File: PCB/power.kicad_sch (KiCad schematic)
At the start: 0 parts

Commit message: Add power supplies
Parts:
- added C27, C30, C33: 10µF, Capacitor_SMD:C_0805_2012Metric, symbol Device:C
- added C28, C29, C31, C32, C34, C35: 22µF, Capacitor_SMD:C_0805_2012Metric, symbol Device:C
- added L1, L2, L3: 2.2µH, Inductor_SMD:L_1210_3225Metric, symbol Device:L
- added R10: 4.75kΩ, Resistor_SMD:R_0402_1005Metric_Pad0.72x0.64mm_HandSolder, symbol Device:R
- added R11: 1.5kΩ, Resistor_SMD:R_0402_1005Metric_Pad0.72x0.64mm_HandSolder, symbol Device:R
- added R12: 1.37kΩ, Resistor_SMD:R_0402_1005Metric_Pad0.72x0.64mm_HandSolder, symbol Device:R
- added R13: 1.65kΩ, Resistor_SMD:R_0402_1005Metric_Pad0.72x0.64mm_HandSolder, symbol Device:R
- added R8: 11.5kΩ, Resistor_SMD:R_0402_1005Metric_Pad0.72x0.64mm_HandSolder, symbol Device:R
- added R9: 2.55kΩ, Resistor_SMD:R_0402_1005Metric_Pad0.72x0.64mm_HandSolder, symbol Device:R
- added U3, U4, U5: TLV62569DBVR, Package_TO_SOT_SMD:SOT-23-5, symbol Regulator_Switching:TLV62569DBV
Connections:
- new net: L3.1, U5.3 (SW)
- new net: L1.1, U3.3 (SW)
- new net: R8.2, R9.1, U3.5 (FB)
- new net: L2.1, U4.3 (SW)
- new net: R10.2, R11.1, U4.5 (FB)
- new net: R12.2, R13.1, U5.5 (FB)
- new net +1V1: C34.1, C35.1, L3.2, R12.1
- new net +2V5: C31.1, C32.1, L2.2, R10.1
- new net +3V3: C28.1, C29.1, L1.2, R8.1
- new net GND: C27.2, C28.2, C29.2, C30.2, C31.2, C32.2, C33.2, C34.2, C35.2, R11.2, R13.2, R9.2, U3.2 (GND), U4.2 (GND), U5.2 (GND)
- new net VBUS: C27.1, C30.1, C33.1, U3.1 (EN), U3.4 (VIN), U4.1 (EN), U4.4 (VIN), U5.1 (EN), U5.4 (VIN)

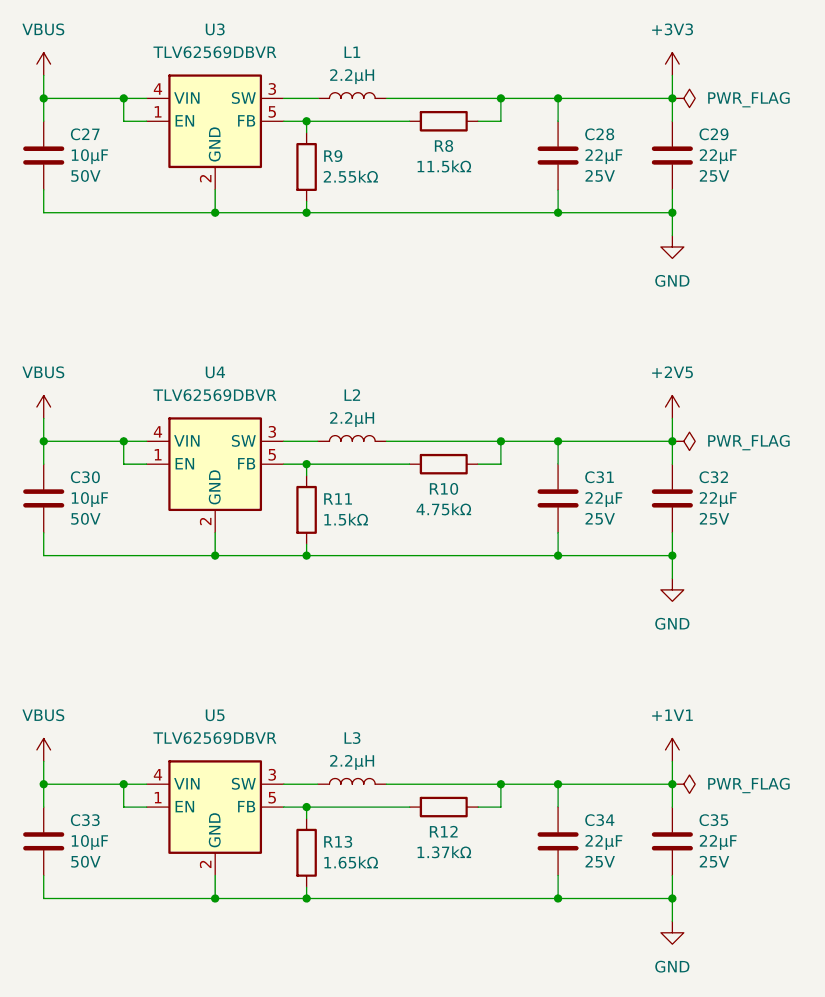
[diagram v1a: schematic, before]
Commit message: Add a USB hub
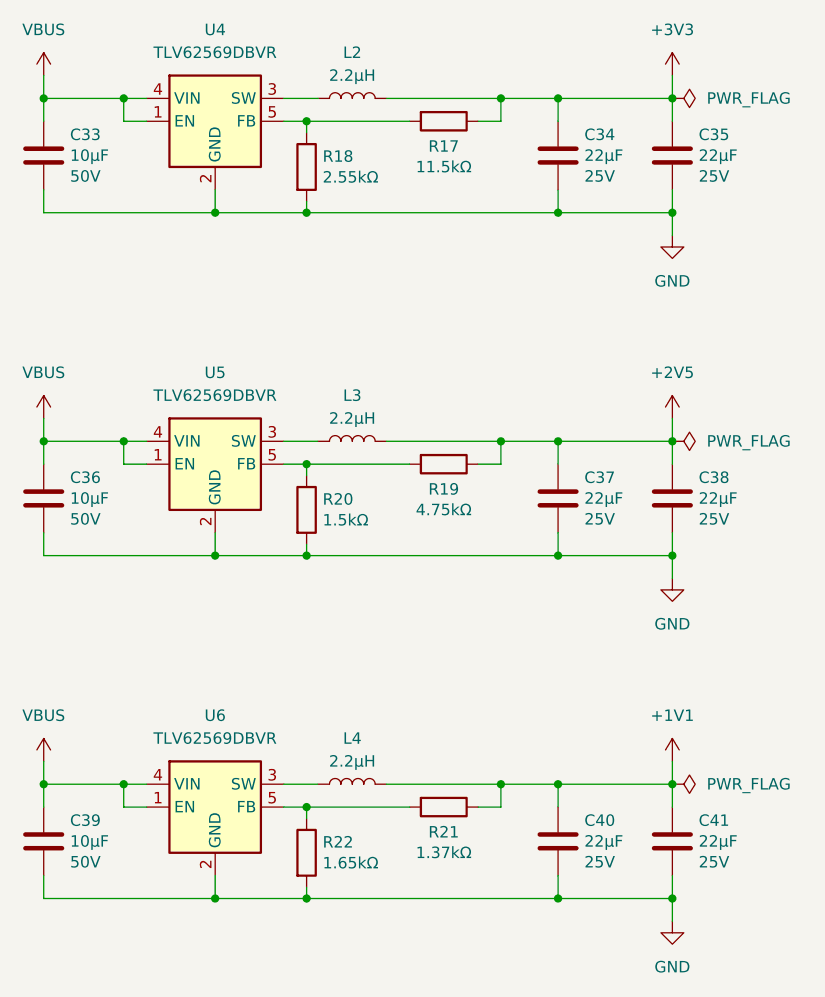
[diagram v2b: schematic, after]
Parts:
- renumbered C27 to C33, C28 to C34, C29 to C35, C30 to C36, C31 to C37, C32 to C38, C33 to C39, C34 to C40, C35 to C41, L1 to L2, L2 to L3, L3 to L4, R8 to R17, R9 to R18, R10 to R19, R11 to R20, R12 to R21, R13 to R22, U3 to U4, U4 to U5, U5 to U6

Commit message: Add the USB to JTAG bridge
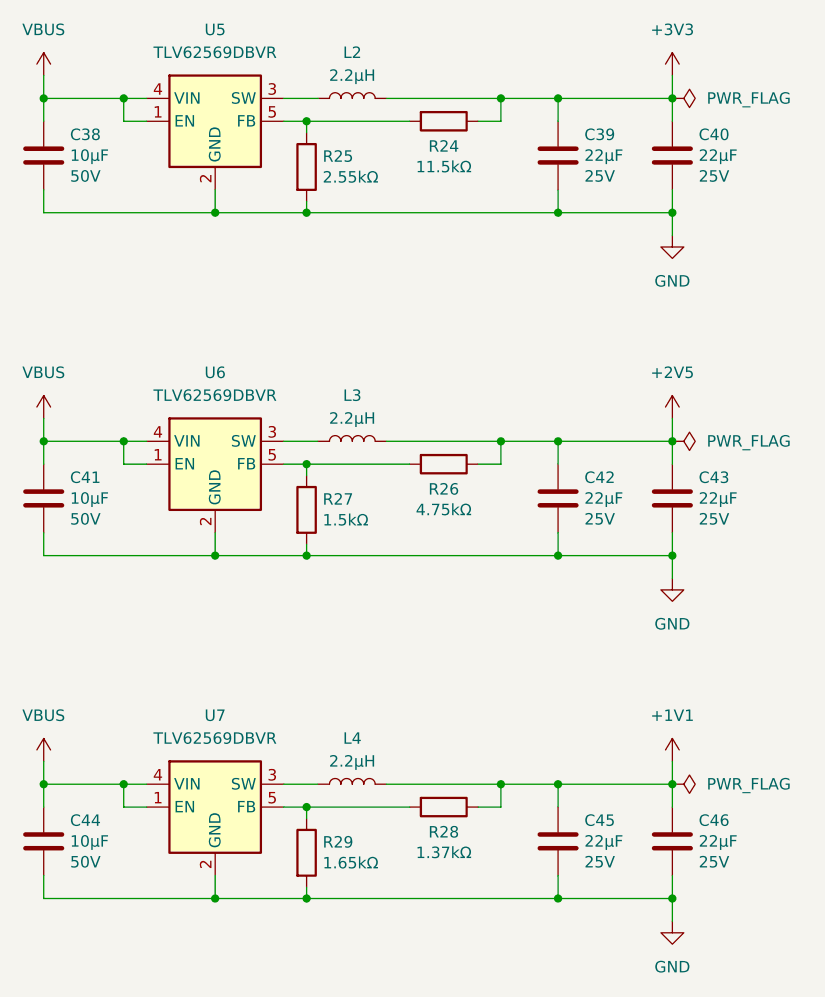
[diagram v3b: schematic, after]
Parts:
- renumbered C33 to C38, C34 to C39, C35 to C40, C36 to C41, C37 to C42, C38 to C43, C39 to C44, C40 to C45, C41 to C46, R17 to R24, R18 to R25, R19 to R26, R20 to R27, R21 to R28, R22 to R29, U4 to U5, U5 to U6, U6 to U7
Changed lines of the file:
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@@
 		(dnp no)
 		(fields_autoplaced yes)
-		(property "Reference" "#PWR060"
+		(property "Reference" "#PWR071"
 			(at 171.45 110.49 0)
 			(effects
@@
 			(project "clavier"
 				(path "/6362c6e0-59ef-40d3-b6e0-7e9dfe7b9b20/0c8a9398-ddd2-4230-9850-fe0f46e922ad"
-					(reference "#PWR060")
+					(reference "#PWR071")
 					(unit 1)
 				)
@@
 		(dnp no)
 		(fields_autoplaced yes)
-		(property "Reference" "U4"
+		(property "Reference" "U5"
 			(at 120.65 43.18 0)
 			(effects
@@
 			(project ""
 				(path "/6362c6e0-59ef-40d3-b6e0-7e9dfe7b9b20/0c8a9398-ddd2-4230-9850-fe0f46e922ad"
-					(reference "U4")
+					(reference "U5")
 					(unit 1)
 				)
@@
 		(dnp no)
 		(fields_autoplaced yes)
-		(property "Reference" "#PWR057"
+		(property "Reference" "#PWR068"
 			(at 171.45 72.39 0)
 			(effects
@@
 			(project "clavier"
 				(path "/6362c6e0-59ef-40d3-b6e0-7e9dfe7b9b20/0c8a9398-ddd2-4230-9850-fe0f46e922ad"
-					(reference "#PWR057")
+					(reference "#PWR068")
 					(unit 1)
 				)
@@
 		(on_board yes)
 		(dnp no)
-		(property "Reference" "R17"
+		(property "Reference" "R24"
 			(at 146.05 56.134 90)
 			(effects
@@
 			(project "clavier"
 				(path "/6362c6e0-59ef-40d3-b6e0-7e9dfe7b9b20/0c8a9398-ddd2-4230-9850-fe0f46e922ad"
-					(reference "R17")
+					(reference "R24")
 					(unit 1)
 				)
@@
 		(dnp no)
 		(fields_autoplaced yes)
-		(property "Reference" "U5"
+		(property "Reference" "U6"
 			(at 120.65 81.28 0)
 			(effects
@@
 			(project "clavier"
 				(path "/6362c6e0-59ef-40d3-b6e0-7e9dfe7b9b20/0c8a9398-ddd2-4230-9850-fe0f46e922ad"
-					(reference "U5")
+					(reference "U6")
 					(unit 1)
 				)
@@
 		(on_board yes)
 		(dnp no)
-		(property "Reference" "C35"
+		(property "Reference" "C40"
 			(at 174.371 54.8386 0)
 			(effects
@@
 			(project "clavier"
 				(path "/6362c6e0-59ef-40d3-b6e0-7e9dfe7b9b20/0c8a9398-ddd2-4230-9850-fe0f46e922ad"
-					(reference "C35")
+					(reference "C40")
 					(unit 1)
 				)
@@
 		(dnp no)
 		(fields_autoplaced yes)
-		(property "Reference" "U6"
+		(property "Reference" "U7"
 			(at 120.65 119.38 0)
 			(effects
@@
 			(project "clavier"
 				(path "/6362c6e0-59ef-40d3-b6e0-7e9dfe7b9b20/0c8a9398-ddd2-4230-9850-fe0f46e922ad"
-					(reference "U6")
+					(reference "U7")
 					(unit 1)
 				)
@@
 		(on_board yes)
 		(dnp no)
-		(property "Reference" "C37"
+		(property "Reference" "C42"
 			(at 161.671 92.9386 0)
 			(effects
@@
 			(project "clavier"
 				(path "/6362c6e0-59ef-40d3-b6e0-7e9dfe7b9b20/0c8a9398-ddd2-4230-9850-fe0f46e922ad"
-					(reference "C37")
+					(reference "C42")
 					(unit 1)
 				)
@@
 		(dnp no)
 		(fields_autoplaced yes)
-		(property "Reference" "#PWR061"
+		(property "Reference" "#PWR072"
 			(at 101.6 128.27 0)
 			(effects
@@
 			(project "clavier"
 				(path "/6362c6e0-59ef-40d3-b6e0-7e9dfe7b9b20/0c8a9398-ddd2-4230-9850-fe0f46e922ad"
-					(reference "#PWR061")
+					(reference "#PWR072")
 					(unit 1)
 				)
@@
 		(on_board yes)
 		(dnp no)
-		(property "Reference" "C33"
+		(property "Reference" "C38"
 			(at 104.521 54.8386 0)
 			(effects
@@
 			(project "clavier"
 				(path "/6362c6e0-59ef-40d3-b6e0-7e9dfe7b9b20/0c8a9398-ddd2-4230-9850-fe0f46e922ad"
-					(reference "C33")
+					(reference "C38")
 					(unit 1)
 				)
@@
 		(dnp no)
 		(fields_autoplaced yes)
-		(property "Reference" "#PWR063"
+		(property "Reference" "#PWR074"
 			(at 171.45 148.59 0)
 			(effects
@@
 			(project "clavier"
 				(path "/6362c6e0-59ef-40d3-b6e0-7e9dfe7b9b20/0c8a9398-ddd2-4230-9850-fe0f46e922ad"
-					(reference "#PWR063")
+					(reference "#PWR074")
 					(unit 1)
 				)
@@
 		(dnp no)
 		(fields_autoplaced yes)
-		(property "Reference" "#PWR055"
+		(property "Reference" "#PWR066"
 			(at 101.6 52.07 0)
 			(effects
@@
 			(project ""
 				(path "/6362c6e0-59ef-40d3-b6e0-7e9dfe7b9b20/0c8a9398-ddd2-4230-9850-fe0f46e922ad"
-					(reference "#PWR055")
+					(reference "#PWR066")
 					(unit 1)
 				)
@@
 		(on_board yes)
 		(dnp no)
-		(property "Reference" "R19"
+		(property "Reference" "R26"
 			(at 146.05 94.234 90)
 			(effects
@@
 			(project "clavier"
 				(path "/6362c6e0-59ef-40d3-b6e0-7e9dfe7b9b20/0c8a9398-ddd2-4230-9850-fe0f46e922ad"
-					(reference "R19")
+					(reference "R26")
 					(unit 1)
 				)
@@
 		(on_board yes)
 		(dnp no)
-		(property "Reference" "R21"
+		(property "Reference" "R28"
 			(at 146.05 132.334 90)
 			(effects
@@
 			(project "clavier"
 				(path "/6362c6e0-59ef-40d3-b6e0-7e9dfe7b9b20/0c8a9398-ddd2-4230-9850-fe0f46e922ad"
-					(reference "R21")
+					(reference "R28")
 					(unit 1)
 				)
@@
 		(dnp no)
 		(fields_autoplaced yes)
-		(property "Reference" "#PWR058"
+		(property "Reference" "#PWR069"
 			(at 101.6 90.17 0)
 			(effects
@@
 			(project "clavier"
 				(path "/6362c6e0-59ef-40d3-b6e0-7e9dfe7b9b20/0c8a9398-ddd2-4230-9850-fe0f46e922ad"
-					(reference "#PWR058")
+					(reference "#PWR069")
 					(unit 1)
 				)
@@
 		(on_board yes)
 		(dnp no)
-		(property "Reference" "R20"
+		(property "Reference" "R27"
 			(at 132.588 95.3516 0)
 			(effects
@@
 			(project "clavier"
 				(path "/6362c6e0-59ef-40d3-b6e0-7e9dfe7b9b20/0c8a9398-ddd2-4230-9850-fe0f46e922ad"
-					(reference "R20")
+					(reference "R27")
 					(unit 1)
 				)
@@
 		(on_board yes)
 		(dnp no)
-		(property "Reference" "C41"
+		(property "Reference" "C46"
 			(at 174.371 131.0386 0)
 			(effects
@@
 			(project "clavier"
 				(path "/6362c6e0-59ef-40d3-b6e0-7e9dfe7b9b20/0c8a9398-ddd2-4230-9850-fe0f46e922ad"
-					(reference "C41")
+					(reference "C46")
 					(unit 1)
 				)
@@
 		(dnp no)
 		(fields_autoplaced yes)
-		(property "Reference" "#PWR056"
+		(property "Reference" "#PWR067"
 			(at 171.45 52.07 0)
 			(effects
@@
 			(project "clavier"
 				(path "/6362c6e0-59ef-40d3-b6e0-7e9dfe7b9b20/0c8a9398-ddd2-4230-9850-fe0f46e922ad"
-					(reference "#PWR056")
+					(reference "#PWR067")
 					(unit 1)
 				)
@@
 		(on_board yes)
 		(dnp no)
-		(property "Reference" "C40"
+		(property "Reference" "C45"
 			(at 161.671 131.0386 0)
 			(effects
@@
 			(project "clavier"
 				(path "/6362c6e0-59ef-40d3-b6e0-7e9dfe7b9b20/0c8a9398-ddd2-4230-9850-fe0f46e922ad"
-					(reference "C40")
+					(reference "C45")
 					(unit 1)
 				)
@@
 		(dnp no)
 		(fields_autoplaced yes)
-		(property "Reference" "#PWR062"
+		(property "Reference" "#PWR073"
 			(at 171.45 128.27 0)
 			(effects
@@
 			(project "clavier"
 				(path "/6362c6e0-59ef-40d3-b6e0-7e9dfe7b9b20/0c8a9398-ddd2-4230-9850-fe0f46e922ad"
-					(reference "#PWR062")
+					(reference "#PWR073")
 					(unit 1)
 				)
@@
 		(on_board yes)
 		(dnp no)
-		(property "Reference" "C34"
+		(property "Reference" "C39"
 			(at 161.671 54.8386 0)
 			(effects
@@
 			(project "clavier"
 				(path "/6362c6e0-59ef-40d3-b6e0-7e9dfe7b9b20/0c8a9398-ddd2-4230-9850-fe0f46e922ad"
-					(reference "C34")
+					(reference "C39")
 					(unit 1)
 				)
@@
 		(on_board yes)
 		(dnp no)
-		(property "Reference" "R22"
+		(property "Reference" "R29"
 			(at 132.588 133.4516 0)
 			(effects
@@
 			(project "clavier"
 				(path "/6362c6e0-59ef-40d3-b6e0-7e9dfe7b9b20/0c8a9398-ddd2-4230-9850-fe0f46e922ad"
-					(reference "R22")
+					(reference "R29")
 					(unit 1)
 				)
@@
 		(on_board yes)
 		(dnp no)
-		(property "Reference" "R18"
+		(property "Reference" "R25"
 			(at 132.588 57.2516 0)
 			(effects
@@
 			(project "clavier"
 				(path "/6362c6e0-59ef-40d3-b6e0-7e9dfe7b9b20/0c8a9398-ddd2-4230-9850-fe0f46e922ad"
-					(reference "R18")
+					(reference "R25")
 					(unit 1)
 				)
@@
 		(on_board yes)
 		(dnp no)
-		(property "Reference" "C39"
+		(property "Reference" "C44"
 			(at 104.521 131.0386 0)
 			(effects
@@
 			(project "clavier"
 				(path "/6362c6e0-59ef-40d3-b6e0-7e9dfe7b9b20/0c8a9398-ddd2-4230-9850-fe0f46e922ad"
-					(reference "C39")
+					(reference "C44")
 					(unit 1)
 				)
@@
 		(on_board yes)
 		(dnp no)
-		(property "Reference" "C36"
+		(property "Reference" "C41"
 			(at 104.521 92.9386 0)
 			(effects
@@
 			(project "clavier"
 				(path "/6362c6e0-59ef-40d3-b6e0-7e9dfe7b9b20/0c8a9398-ddd2-4230-9850-fe0f46e922ad"
-					(reference "C36")
+					(reference "C41")
 					(unit 1)
 				)
@@
 		(dnp no)
 		(fields_autoplaced yes)
-		(property "Reference" "#PWR059"
+		(property "Reference" "#PWR070"
 			(at 171.45 90.17 0)
 			(effects
@@
 			(project "clavier"
 				(path "/6362c6e0-59ef-40d3-b6e0-7e9dfe7b9b20/0c8a9398-ddd2-4230-9850-fe0f46e922ad"
-					(reference "#PWR059")
+					(reference "#PWR070")
 					(unit 1)
 				)
@@
 		(on_board yes)
 		(dnp no)
-		(property "Reference" "C38"
+		(property "Reference" "C43"
 			(at 174.371 92.9386 0)
 			(effects
@@
 			(project "clavier"
 				(path "/6362c6e0-59ef-40d3-b6e0-7e9dfe7b9b20/0c8a9398-ddd2-4230-9850-fe0f46e922ad"
-					(reference "C38")
-					(unit 1)
-				)
+					(reference "C43")
+					(unit 1)
+				)
